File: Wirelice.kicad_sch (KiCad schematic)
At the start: 32 parts, among them J1 SWD, J2 USB_C_Receptacle_USB2.0, J3 Unified DB, J5 Battery, SW29 SW_Push, U1 nRF52840_holyiot_18010, U2 SRV05-4, U3 TP4056, U4 FS8205, U5 DW01A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

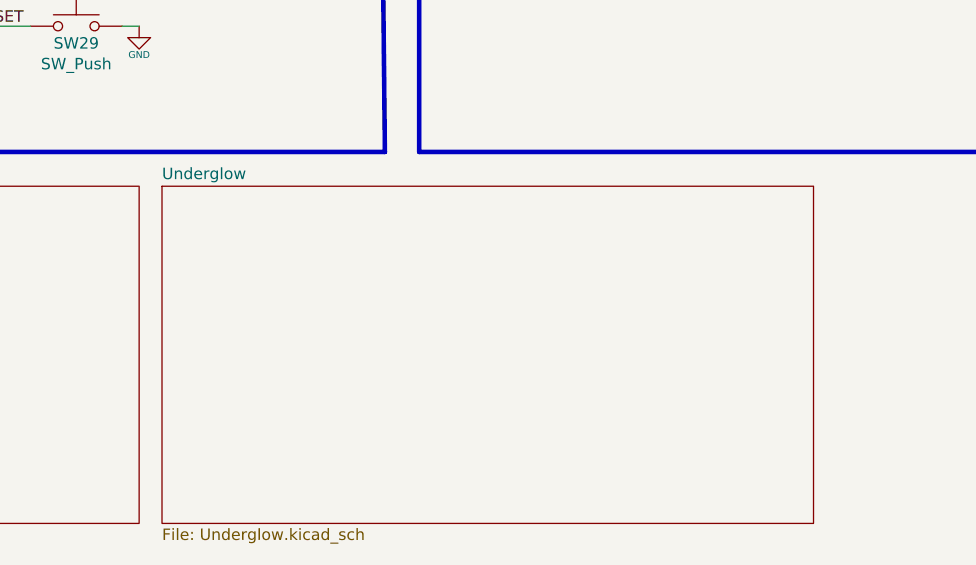
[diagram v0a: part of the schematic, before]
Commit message: Removed LEDS and updated holes
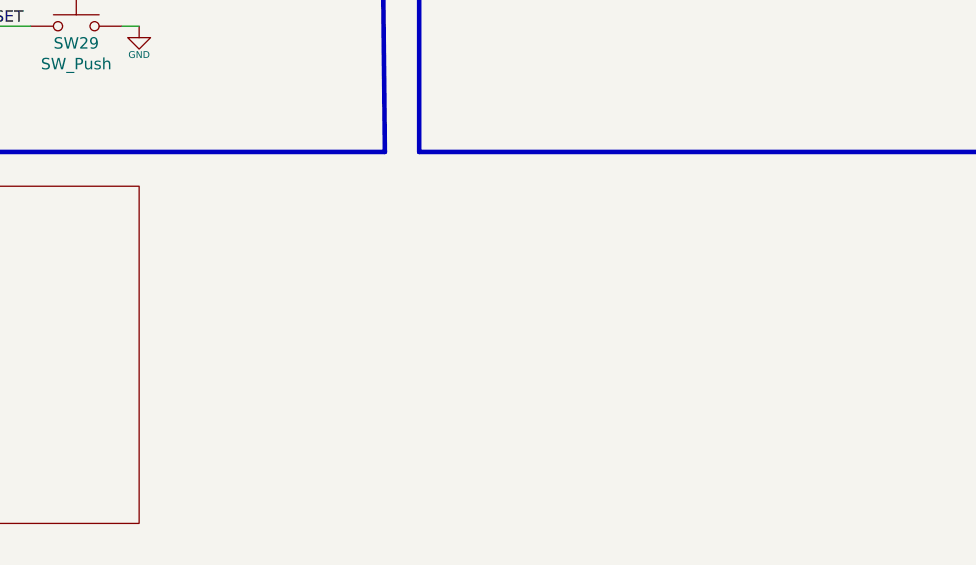
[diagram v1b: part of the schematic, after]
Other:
- removed sheet Underglow
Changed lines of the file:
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@@
-    )
-  )
-  (sheet (at 92.71 143.51) (size 72.39 37.465) (fields_autoplaced)
-    (stroke (width 0.0006) (type solid) (color 0 0 0 0))
-    (fill (color 0 0 0 0.0000))
-    (property "Sheet name" "Underglow" (id 0) (at 92.71 142.8743 0)
-      (effects (font (size 1.27 1.27)) (justify left bottom))
-    )
-    (property "Sheet file" "Underglow.kicad_sch" (id 1) (at 92.71 181.4837 0)
-      (effects (font (size 1.27 1.27)) (justify left top))
     )
   )
@@
     (path "/" (page "1"))
     (path "/3738995a-4258-4edd-9202-963ed7000583/" (page " "))
-    (path "/aa7af192-2f2d-4ff7-9fb0-e8b87c3f1236/" (page " "))
   )
   (symbol_instances
@@
       (reference "MX73") (unit 1) (value "2uLSpace") (footprint "MX_Only:MXOnly-2U-ReversedStabilizers-NoLED")
     )
-    (path "/aa7af192-2f2d-4ff7-9fb0-e8b87c3f1236/71307b41-dd54-4756-824b-e54f4ce13d95"
-      (reference "#PWR0106") (unit 1) (value "GND") (footprint "")
-    )
-    (path "/aa7af192-2f2d-4ff7-9fb0-e8b87c3f1236/130f2382-5b65-4caa-b256-b006b28ec9f7"
-      (reference "#PWR0112") (unit 1) (value "GND") (footprint "")
-    )
-    (path "/aa7af192-2f2d-4ff7-9fb0-e8b87c3f1236/77944356-941c-43b4-8360-871cc64c58a9"
-      (reference "#PWR0113") (unit 1) (value "GND") (footprint "")
-    )
-    (path "/aa7af192-2f2d-4ff7-9fb0-e8b87c3f1236/80c33b0b-7ae5-4bc4-b7b0-2f004d572cbe"
-      (reference "#PWR0114") (unit 1) (value "GND") (footprint "")
-    )
-    (path "/aa7af192-2f2d-4ff7-9fb0-e8b87c3f1236/d3cc8a69-76e7-4359-a12c-02b6c46dfd43"
-      (reference "#PWR0115") (unit 1) (value "+3.3V") (footprint "")
-    )
-    (path "/aa7af192-2f2d-4ff7-9fb0-e8b87c3f1236/a9c4fa3c-6ff4-4989-bbee-3ed2618404e7"
-      (reference "#PWR0116") (unit 1) (value "GND") (footprint "")
-    )
-    (path "/aa7af192-2f2d-4ff7-9fb0-e8b87c3f1236/37a182af-9249-41b9-8b6e-94600341b3c6"
-      (reference "C1") (unit 1) (value "100nF") (footprint "Capacitor_SMD:C_0603_1608Metric")
-    )
-    (path "/aa7af192-2f2d-4ff7-9fb0-e8b87c3f1236/c6a189ae-3cff-4eb4-8aa1-905cd1f101b0"
-      (reference "C2") (unit 1) (value "100nF") (footprint "Capacitor_SMD:C_0603_1608Metric")
-    )
-    (path "/aa7af192-2f2d-4ff7-9fb0-e8b87c3f1236/91c9aa05-7792-4285-923b-4f2773c2ef27"
-      (reference "C3") (unit 1) (value "100nF") (footprint "Capacitor_SMD:C_0603_1608Metric")
-    )
-    (path "/aa7af192-2f2d-4ff7-9fb0-e8b87c3f1236/94a8449f-95c1-448f-aefc-7914848110ca"
-      (reference "C4") (unit 1) (value "100nF") (footprint "Capacitor_SMD:C_0603_1608Metric")
-    )
-    (path "/aa7af192-2f2d-4ff7-9fb0-e8b87c3f1236/e7fdcccb-f287-438a-8219-8edc6fa5fdae"
-      (reference "C5") (unit 1) (value "100nF") (footprint "Capacitor_SMD:C_0603_1608Metric")
-    )
-    (path "/aa7af192-2f2d-4ff7-9fb0-e8b87c3f1236/080e36ac-bcf5-4676-a6df-991d69735f0a"
-      (reference "C6") (unit 1) (value "100nF") (footprint "Capacitor_SMD:C_0603_1608Metric")
-    )
-    (path "/aa7af192-2f2d-4ff7-9fb0-e8b87c3f1236/0f94d603-6f20-439f-aec5-d721a17e461e"
-      (reference "C7") (unit 1) (value "100nF") (footprint "Capacitor_SMD:C_0603_1608Metric")
-    )
-    (path "/aa7af192-2f2d-4ff7-9fb0-e8b87c3f1236/f911fe44-a4bc-4143-952b-b5fc4b259df5"
-      (reference "C8") (unit 1) (value "100nF") (footprint "Capacitor_SMD:C_0603_1608Metric")
-    )
-    (path "/aa7af192-2f2d-4ff7-9fb0-e8b87c3f1236/6c3ee1c2-a450-47e3-9158-9069ff81930b"
-      (reference "C9") (unit 1) (value "100nF") (footprint "Capacitor_SMD:C_0603_1608Metric")
-    )
-    (path "/aa7af192-2f2d-4ff7-9fb0-e8b87c3f1236/ddea06a0-460c-4854-8c71-634840b7ba20"
-      (reference "C10") (unit 1) (value "100nF") (footprint "Capacitor_SMD:C_0603_1608Metric")
-    )
-    (path "/aa7af192-2f2d-4ff7-9fb0-e8b87c3f1236/c1ed69fe-774d-4453-adae-83a2a5e69149"
-      (reference "C13") (unit 1) (value "100nF") (footprint "Capacitor_SMD:C_0603_1608Metric")
-    )
-    (path "/aa7af192-2f2d-4ff7-9fb0-e8b87c3f1236/798777e0-ef29-4295-b425-d9554ff2be26"
-      (reference "C15") (unit 1) (value "100nF") (footprint "Capacitor_SMD:C_0603_1608Metric")
-    )
-    (path "/aa7af192-2f2d-4ff7-9fb0-e8b87c3f1236/49af69f5-7acd-43f7-aa72-9341def5dd0e"
-      (reference "C16") (unit 1) (value "100nF") (footprint "Capacitor_SMD:C_0603_1608Metric")
-    )
-    (path "/aa7af192-2f2d-4ff7-9fb0-e8b87c3f1236/1c48e722-1c92-4031-887a-d68c6dcabf98"
-      (reference "C17") (unit 1) (value "100nF") (footprint "Capacitor_SMD:C_0603_1608Metric")
-    )
-    (path "/aa7af192-2f2d-4ff7-9fb0-e8b87c3f1236/db3e763b-48b9-4819-a27d-459216cca55e"
-      (reference "D2") (unit 1) (value "SK6812MINI") (footprint "LED_SMD:LED_SK6812MINI_PLCC4_3.5x3.5mm_P1.75mm")
-    )
-    (path "/aa7af192-2f2d-4ff7-9fb0-e8b87c3f1236/81b73469-fd17-4134-9bf9-7d3028d331b3"
-      (reference "D3") (unit 1) (value "SK6812MINI") (footprint "LED_SMD:LED_SK6812MINI_PLCC4_3.5x3.5mm_P1.75mm")
-    )
-    (path "/aa7af192-2f2d-4ff7-9fb0-e8b87c3f1236/79dc0279-dc74-447c-adf2-122886d4f75a"
-      (reference "D4") (unit 1) (value "SK6812MINI") (footprint "LED_SMD:LED_SK6812MINI_PLCC4_3.5x3.5mm_P1.75mm")
-    )
-    (path "/aa7af192-2f2d-4ff7-9fb0-e8b87c3f1236/6615dd8e-8498-45a2-adc7-bf326b4f0894"
-      (reference "D5") (unit 1) (value "SK6812MINI") (footprint "LED_SMD:LED_SK6812MINI_PLCC4_3.5x3.5mm_P1.75mm")
-    )
-    (path "/aa7af192-2f2d-4ff7-9fb0-e8b87c3f1236/fb397c04-1d8d-493f-8032-7ba22c865701"
-      (reference "D6") (unit 1) (value "SK6812MINI") (footprint "LED_SMD:LED_SK6812MINI_PLCC4_3.5x3.5mm_P1.75mm")
-    )
-    (path "/aa7af192-2f2d-4ff7-9fb0-e8b87c3f1236/213f276a-b576-418b-b886-206d5299ae1d"
-      (reference "D7") (unit 1) (value "SK6812MINI") (footprint "LED_SMD:LED_SK6812MINI_PLCC4_3.5x3.5mm_P1.75mm")
-    )
-    (path "/aa7af192-2f2d-4ff7-9fb0-e8b87c3f1236/51f99943-e697-482e-a89c-f66d32f100c9"
-      (reference "D8") (unit 1) (value "SK6812MINI") (footprint "LED_SMD:LED_SK6812MINI_PLCC4_3.5x3.5mm_P1.75mm")
-    )
-    (path "/aa7af192-2f2d-4ff7-9fb0-e8b87c3f1236/4418a6b3-50ec-45d7-b4d5-ba031ec06c51"
-      (reference "D9") (unit 1) (value "SK6812MINI") (footprint "LED_SMD:LED_SK6812MINI_PLCC4_3.5x3.5mm_P1.75mm")
-    )
-    (path "/aa7af192-2f2d-4ff7-9fb0-e8b87c3f1236/73dd11d8-b425-48bc-afcd-83cf4a22ec21"
-      (reference "D10") (unit 1) (value "SK6812MINI") (footprint "LED_SMD:LED_SK6812MINI_PLCC4_3.5x3.5mm_P1.75mm")
-    )
-    (path "/aa7af192-2f2d-4ff7-9fb0-e8b87c3f1236/862f6c80-dc0e-4ddd-bdca-86841150c616"
-      (reference "D11") (unit 1) (value "SK6812MINI") (footprint "LED_SMD:LED_SK6812MINI_PLCC4_3.5x3.5mm_P1.75mm")
-    )
-    (path "/aa7af192-2f2d-4ff7-9fb0-e8b87c3f1236/e6184029-a648-4699-b52a-d9d5e19b44d4"
-      (reference "D12") (unit 1) (value "SK6812MINI") (footprint "LED_SMD:LED_SK6812MINI_PLCC4_3.5x3.5mm_P1.75mm")
-    )
-    (path "/aa7af192-2f2d-4ff7-9fb0-e8b87c3f1236/f661792e-ba69-48d5-9fa5-f9e5fd74d142"
-      (reference "D13") (unit 1) (value "SK6812MINI") (footprint "LED_SMD:LED_SK6812MINI_PLCC4_3.5x3.5mm_P1.75mm")
-    )
-    (path "/aa7af192-2f2d-4ff7-9fb0-e8b87c3f1236/b5ce496e-faa5-4870-8b70-f624781e4f71"
-      (reference "Q1") (unit 1) (value "2N7002") (footprint "Package_TO_SOT_SMD:SOT-23")
-    )
-    (path "/aa7af192-2f2d-4ff7-9fb0-e8b87c3f1236/155a01ab-f14f-4490-8bff-8f322ffec1b6"
-      (reference "Q2") (unit 1) (value "AO3401A") (footprint "Package_TO_SOT_SMD:SOT-23")
-    )
-    (path "/aa7af192-2f2d-4ff7-9fb0-e8b87c3f1236/3447faa2-2e84-4f4a-afbb-061dcd2cc244"
-      (reference "R6") (unit 1) (value "100R") (footprint "Resistor_SMD:R_0603_1608Metric")
-    )
-    (path "/aa7af192-2f2d-4ff7-9fb0-e8b87c3f1236/08a595d9-d7a5-4e7b-9253-f41471203e94"
-      (reference "R9") (unit 1) (value "10k") (footprint "Resistor_SMD:R_0603_1608Metric")
-    )
-    (path "/aa7af192-2f2d-4ff7-9fb0-e8b87c3f1236/14a6b1b2-bb29-4b57-8020-1ff102095e1f"
-      (reference "R10") (unit 1) (value "10k") (footprint "Resistor_SMD:R_0603_1608Metric")
-    )
-    (path "/aa7af192-2f2d-4ff7-9fb0-e8b87c3f1236/d44d3f82-55de-4957-ad2e-42e1d66a95e6"
-      (reference "R11") (unit 1) (value "10k") (footprint "Resistor_SMD:R_0603_1608Metric")
-    )
-    (path "/aa7af192-2f2d-4ff7-9fb0-e8b87c3f1236/2f8ecbda-589d-4e77-8204-93ff67839d48"
-      (reference "U7") (unit 1) (value "TXS0101") (footprint "Package_TO_SOT_SMD:SOT-363_SC-70-6")
-    )
   )

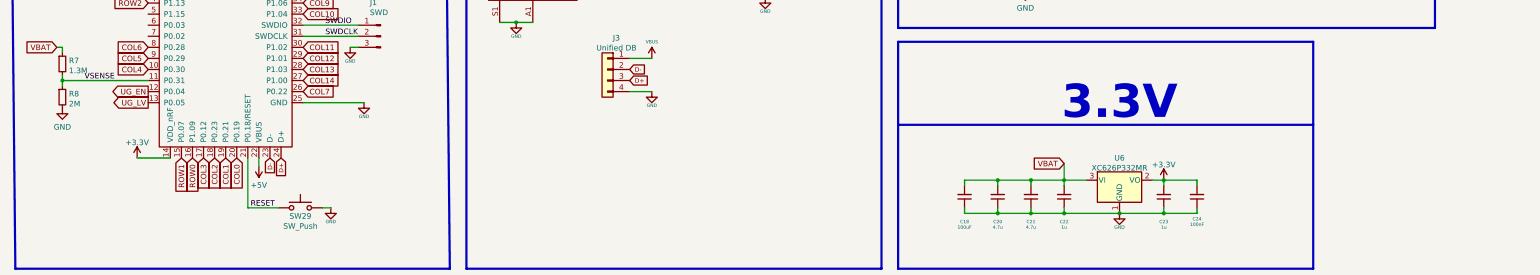
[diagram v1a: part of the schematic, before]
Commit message: Compacted components and removed RGBs
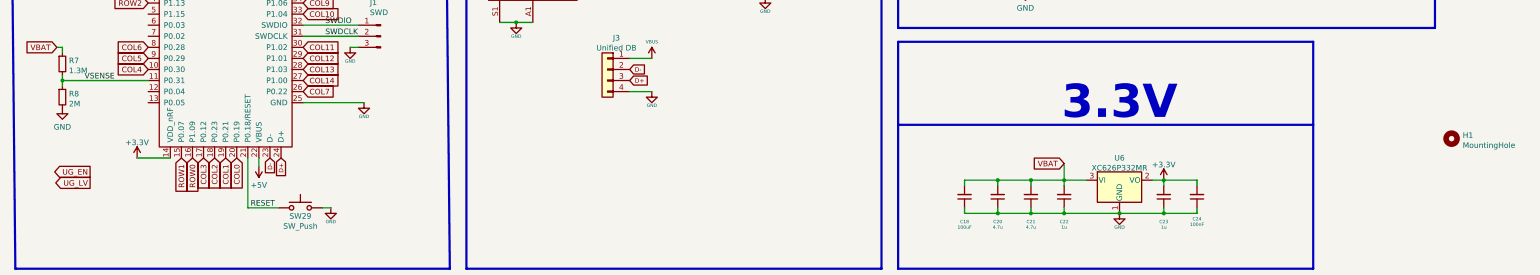
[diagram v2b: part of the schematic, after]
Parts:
- added H1: MountingHole, sleep-lib:noun_geometric pattern_889496, symbol Mechanical:MountingHole
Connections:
- net UG_EN: no longer U1.12 (P0.04)
- net UG_LV: no longer U1.13 (P0.05)
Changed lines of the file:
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@@
+    )
+  )
+  (global_label "UG_EN" (shape output) (at 34.925 117.475 180) (fields_autoplaced)
+    (effects (font (size 1.27 1.27)) (justify right))
+    (property "Intersheet References" "${INTERSHEET_REFS}" (id 0) (at 26.4643 117.5544 0)
+      (effects (font (size 1.27 1.27)) (justify right) hide)
+    )
+  )
+  (global_label "UG_LV" (shape output) (at 34.925 120.015 180) (fields_autoplaced)
+    (effects (font (size 1.27 1.27)) (justify right))
+    (property "Intersheet References" "${INTERSHEET_REFS}" (id 0) (at 26.8271 119.9356 0)
+      (effects (font (size 1.27 1.27)) (justify right) hide)
     )
   )
@@
     (effects (font (size 1.27 1.27)) (justify right))
     (property "Intersheet References" "${INTERSHEET_REFS}" (id 0) (at 182.88 -235.585 0)
-      (effects (font (size 1.27 1.27)) (justify right) hide)
-    )
-  )
-  (global_label "UG_EN" (shape output) (at 48.26 99.06 180) (fields_autoplaced)
-    (effects (font (size 1.27 1.27)) (justify right))
-    (property "Intersheet References" "${INTERSHEET_REFS}" (id 0) (at 39.7993 99.1394 0)
-      (effects (font (size 1.27 1.27)) (justify right) hide)
-    )
-  )
-  (global_label "UG_LV" (shape output) (at 48.26 101.6 180) (fields_autoplaced)
-    (effects (font (size 1.27 1.27)) (justify right))
-    (property "Intersheet References" "${INTERSHEET_REFS}" (id 0) (at 40.1621 101.5206 0)
       (effects (font (size 1.27 1.27)) (justify right) hide)
     )
@@
     (pin "1")
     (pin "2")
+  )
+  (symbol (lib_id "Mechanical:MountingHole") (at 347.345 109.855 0) (unit 1)
+    (in_bom yes) (on_board yes) (fields_autoplaced)
+    (property "Reference" "H1" (id 0) (at 349.8851 109.0941 0)
+      (effects (font (size 1.27 1.27)) (justify left))
+    )
+    (property "Value" "MountingHole" (id 1) (at 349.8851 111.3928 0)
+      (effects (font (size 1.27 1.27)) (justify left))
+    )
+    (property "Footprint" "sleep-lib:noun_geometric pattern_889496" (id 2) (at 347.345 109.855 0)
+      (effects (font (size 1.27 1.27)) hide)
+    )
+    (property "Datasheet" "~" (id 3) (at 347.345 109.855 0)
+      (effects (font (size 1.27 1.27)) hide)
+    )
   )
   (symbol (lib_id "Device:CP_Small") (at 243.205 52.705 0) (unit 1)
@@
       (reference "F1") (unit 1) (value "750mA") (footprint "Fuse:Fuse_0603_1608Metric")
     )
+    (path "/6bdd9235-0eba-47c7-b2db-4bd34a7723e4"
+      (reference "H1") (unit 1) (value "MountingHole") (footprint "sleep-lib:noun_geometric pattern_889496")
+    )
     (path "/1eb60322-c6a4-4376-9ba4-cf176bd3fe18"

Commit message: Updated things
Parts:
- added C1: 100nF, Capacitor_SMD:C_0603_1608Metric, symbol Device:C_Small
- added FB1: Ferrite Bead, Inductor_SMD:L_0805_2012Metric, symbol Device:Ferrite_Bead_Small
- C18: symbol Device:C_Small -> Device:CP_Small
- D64: footprint LED_THT:LED_D3.0mm -> LED_SMD:LED_0805_2012Metric; LCSC (none) -> C2297
- D65: footprint LED_THT:LED_D3.0mm -> LED_SMD:LED_0805_2012Metric; LCSC (none) -> C84256
- H1: value MountingHole -> Logo; footprint sleep-lib:noun_geometric pattern_889496 -> sleep-lib:logo-large-CU; now left out of the parts list
- J1: symbol Connector:Conn_01x03_Male -> Connector_Generic:Conn_01x03; now left out of the parts list
- J3: LCSC (none) -> C160404
- J5: footprint Connector_JST:JST_SH_SM02B-SRSS-TB_1x02-1MP_P1.00mm_Horizontal -> Connector_JST:JST_PH_S2B-PH-SM4-TB_1x02-1MP_P2.00mm_Horizontal; now left out of the parts list
- SW29: now left out of the parts list
- U3: footprint sleep-lib:SOP-8 -> Package_SO:SOIC-8-1EP_3.9x4.9mm_P1.27mm_EP2.29x3mm
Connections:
- net COL4: now also U1.8 (P0.28); no longer U1.10 (P0.30)
- net COL5: now also U1.7 (P0.02); no longer U1.9 (P0.29)
- net COL6: now also U1.6 (P0.03); no longer U1.8 (P0.28)
- net GND: now also C18.2, J1.1 (Pin_1), FB1.1; no longer C18.1, J1.3 (Pin_3), J2.S1 (SHIELD)
- net SWDIO: now also J1.3 (Pin_3); no longer J1.1 (Pin_1)
- net VBAT: now also C18.1; no longer C18.2
- net CSI: now reaches R5.1, U5.2 (CSI)
- net at J5.1 (Pin_1), U4.1 (S1), U5.6 (VSS): now also C1.1
- net OC: now reaches U4.4 (G2), U5.3 (OC)
- net OD: now reaches U4.6 (G1), U5.1 (OD)
- net at R4.1, U5.5 (VDD): now also C1.2
- net EXTRA4: now reaches U1.36 (P0.10)
- net PROG: now reaches R3.1, U3.2 (PROG)
- new net ENCA: U1.9 (P0.29)
- new net ENCB: U1.10 (P0.30)
- new net GNDPWR: FB1.2, J2.S1 (SHIELD)
- no-connect marks 24 -> 27
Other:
- note added: "Extra"
- note added: "Pins 0.04 and 0.05 reserved for underglow Unerglow sheet already exists, named Underglow.kicad_sch"
- moved on the sheet: H1, J3
